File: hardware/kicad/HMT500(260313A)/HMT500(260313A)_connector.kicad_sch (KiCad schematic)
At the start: 10 parts, among them J1 SM08B-GHS-TB, J5 Chassis contact

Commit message: Schematic: global label shape shows signal direction (driver = output, receiver = input)
Direction derived per net from pin types (output / tri-state / open-drain
drivers, MCU as driver when only inputs are on the other side); analog
and passive nets keep the plain shape, RS-485 bus bidirectional.
Legend line on the root sheet; test for key nets.

Co-Authored-By: Claude Opus 5.5 <noreply@anthropic.com>
Claude-Session: https://claude.ai/code/session_01JA2o8uJsqp9Vzsg4b665ev
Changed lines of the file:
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@@
 (global_label "OUT1_EXT" (shape passive) (at 58.42 76.2 0) (fields_autoplaced) (effects (font (size 1.27 1.27)) (justify left)) (property "Intersheetrefs" "${INTERSHEET_REFS}" (at 58.42 76.2 0) (effects (font (size 1.27 1.27)) hide)))
 (global_label "OUT2_EXT" (shape passive) (at 58.42 78.74 0) (fields_autoplaced) (effects (font (size 1.27 1.27)) (justify left)) (property "Intersheetrefs" "${INTERSHEET_REFS}" (at 58.42 78.74 0) (effects (font (size 1.27 1.27)) hide)))
-(global_label "RS485_A_EXT" (shape passive) (at 58.42 81.28 0) (fields_autoplaced) (effects (font (size 1.27 1.27)) (justify left)) (property "Intersheetrefs" "${INTERSHEET_REFS}" (at 58.42 81.28 0) (effects (font (size 1.27 1.27)) hide)))
-(global_label "RS485_B_EXT" (shape passive) (at 58.42 83.82 0) (fields_autoplaced) (effects (font (size 1.27 1.27)) (justify left)) (property "Intersheetrefs" "${INTERSHEET_REFS}" (at 58.42 83.82 0) (effects (font (size 1.27 1.27)) hide)))
+(global_label "RS485_A_EXT" (shape bidirectional) (at 58.42 81.28 0) (fields_autoplaced) (effects (font (size 1.27 1.27)) (justify left)) (property "Intersheetrefs" "${INTERSHEET_REFS}" (at 58.42 81.28 0) (effects (font (size 1.27 1.27)) hide)))
+(global_label "RS485_B_EXT" (shape bidirectional) (at 58.42 83.82 0) (fields_autoplaced) (effects (font (size 1.27 1.27)) (justify left)) (property "Intersheetrefs" "${INTERSHEET_REFS}" (at 58.42 83.82 0) (effects (font (size 1.27 1.27)) hide)))
 (no_connect (at 55.88 86.36))
 (no_connect (at 55.88 88.9))

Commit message: Schematic: wire nearby same-sheet nets, signal-flow direction for analog nets
- Analog: +VSENSE and terminal feedback drawn as wires to the OPA197
  buffer (no DACn_SENSE / second OUTn_EXT labels); U14 1A/2A tied, one
  DAC_SCK label
- Power: TPS2660 left pins reordered so R3-R5 run straight from IN to
  UVLO/OVP; one VIN_F label
- Measurement: C27 sits directly between R17/R18 and AIN1/AIN2
- MCU: SWD pads (J2) placed on the PA13/PA14 rows and wired directly
- Label direction for passive nets from signal flow: OUTn_EXT analog ->
  connector, VIN_F connector -> eFuse, BUCK_FB divider -> FB
- Tests: nearby same-sheet labels must be wired; bend limit 6/sheet;
  check_netlist accepts KiCad auto-named multi-pin nets

Co-Authored-By: Claude Opus 5.5 <noreply@anthropic.com>
Claude-Session: https://claude.ai/code/session_01JA2o8uJsqp9Vzsg4b665ev
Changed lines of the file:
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@@
 (wire (pts (xy 137.16 114.3) (xy 137.16 116.84)) (stroke (width 0) (type default)))
 (wire (pts (xy 137.16 124.46) (xy 137.16 127)) (stroke (width 0) (type default)))
-(global_label "VIN_F" (shape passive) (at 182.88 71.12 0) (fields_autoplaced) (effects (font (size 1.27 1.27)) (justify left)) (property "Intersheetrefs" "${INTERSHEET_REFS}" (at 182.88 71.12 0) (effects (font (size 1.27 1.27)) hide)))
-(global_label "OUT1_EXT" (shape passive) (at 58.42 76.2 0) (fields_autoplaced) (effects (font (size 1.27 1.27)) (justify left)) (property "Intersheetrefs" "${INTERSHEET_REFS}" (at 58.42 76.2 0) (effects (font (size 1.27 1.27)) hide)))
-(global_label "OUT2_EXT" (shape passive) (at 58.42 78.74 0) (fields_autoplaced) (effects (font (size 1.27 1.27)) (justify left)) (property "Intersheetrefs" "${INTERSHEET_REFS}" (at 58.42 78.74 0) (effects (font (size 1.27 1.27)) hide)))
+(global_label "VIN_F" (shape output) (at 182.88 71.12 0) (fields_autoplaced) (effects (font (size 1.27 1.27)) (justify left)) (property "Intersheetrefs" "${INTERSHEET_REFS}" (at 182.88 71.12 0) (effects (font (size 1.27 1.27)) hide)))
+(global_label "OUT1_EXT" (shape input) (at 58.42 76.2 0) (fields_autoplaced) (effects (font (size 1.27 1.27)) (justify left)) (property "Intersheetrefs" "${INTERSHEET_REFS}" (at 58.42 76.2 0) (effects (font (size 1.27 1.27)) hide)))
+(global_label "OUT2_EXT" (shape input) (at 58.42 78.74 0) (fields_autoplaced) (effects (font (size 1.27 1.27)) (justify left)) (property "Intersheetrefs" "${INTERSHEET_REFS}" (at 58.42 78.74 0) (effects (font (size 1.27 1.27)) hide)))
 (global_label "RS485_A_EXT" (shape bidirectional) (at 58.42 81.28 0) (fields_autoplaced) (effects (font (size 1.27 1.27)) (justify left)) (property "Intersheetrefs" "${INTERSHEET_REFS}" (at 58.42 81.28 0) (effects (font (size 1.27 1.27)) hide)))
 (global_label "RS485_B_EXT" (shape bidirectional) (at 58.42 83.82 0) (fields_autoplaced) (effects (font (size 1.27 1.27)) (justify left)) (property "Intersheetrefs" "${INTERSHEET_REFS}" (at 58.42 83.82 0) (effects (font (size 1.27 1.27)) hide)))

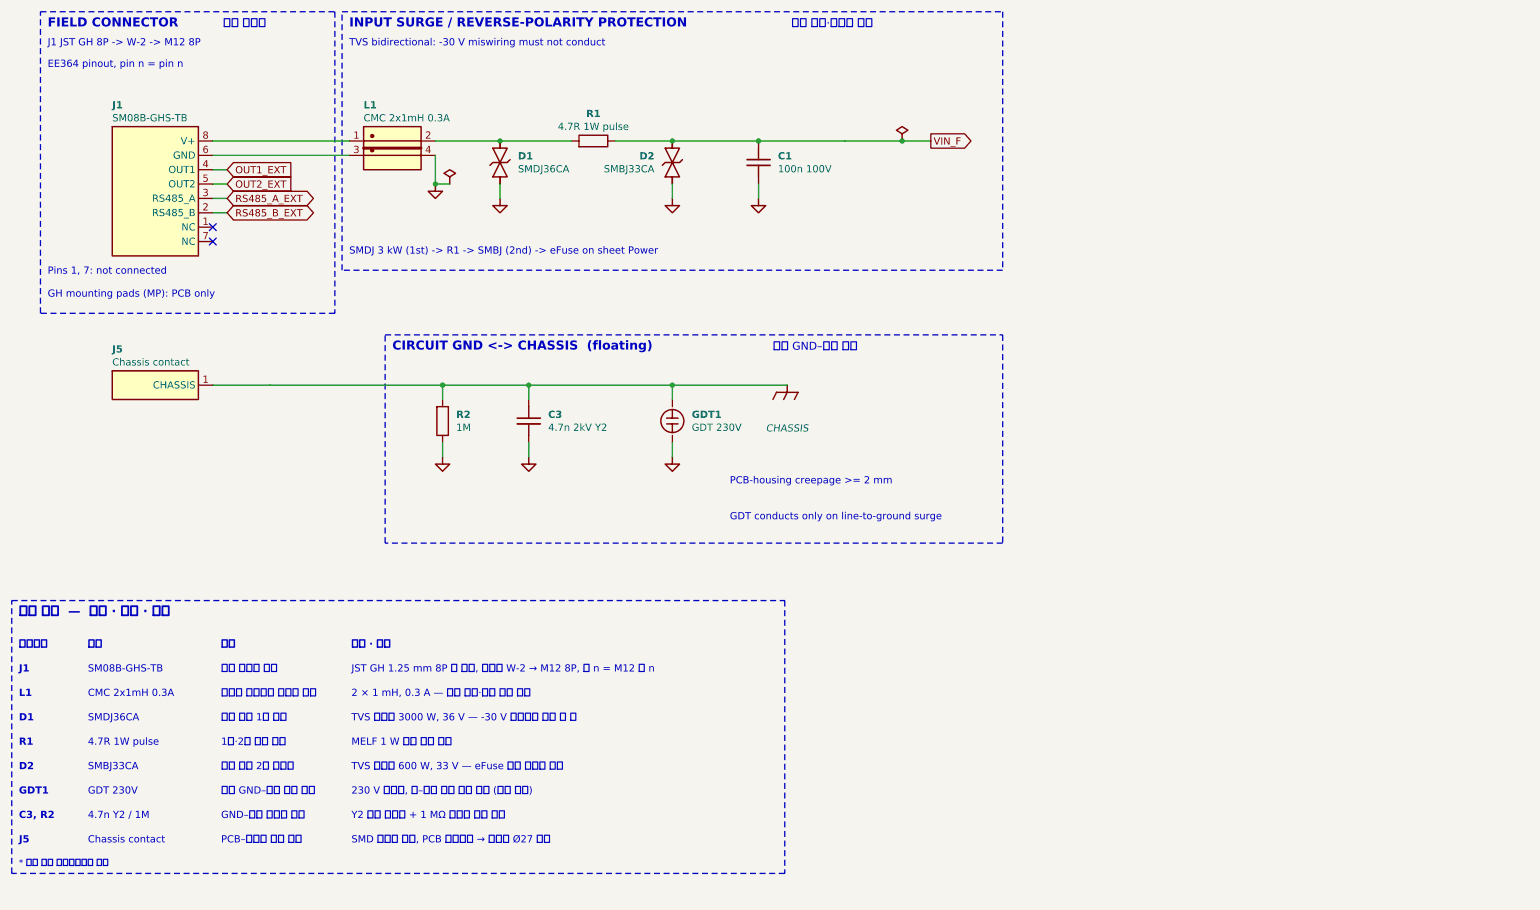
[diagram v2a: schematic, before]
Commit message: Footprints and part numbers: no TBD left in the schematic
- Project footprint library hardware/kicad/lib/HMT500_260313A.pretty:
  KiCad 7.0.11 footprints + gen_footprints.py (LMR36006 RNX0012A from TI
  land pattern, Bourns 2035-xx-SM GDT, TVS3301 DRB with floating pad)
- GDT changed to 2-electrode Bourns 2035-23-SM-RPLF (2038 is 3-electrode)
- L1 Wurth WE-SL2 744222 (1 mH, 0.8 A); CMC pins renumbered to WE-SL2
  windings 1-4 / 2-3
- J5 Harwin S1941-46R, L2 Coilcraft XGL4030-153MEC, TPS26611 SOT-23-8,
  TPS2660 HTSSOP-16 footprint from 7.0.11
- R1 MMB02070C4708FB200, R30/R40 CRCW251210R0FKEGHP confirmed;
  R19 -> Vishay PLTT0603 0.02 % 5 ppm
- fp-lib-table written by the generator; netlist 74/74, tests pass

Co-Authored-By: Claude Opus 5.5 <noreply@anthropic.com>
Claude-Session: https://claude.ai/code/session_01JA2o8uJsqp9Vzsg4b665ev
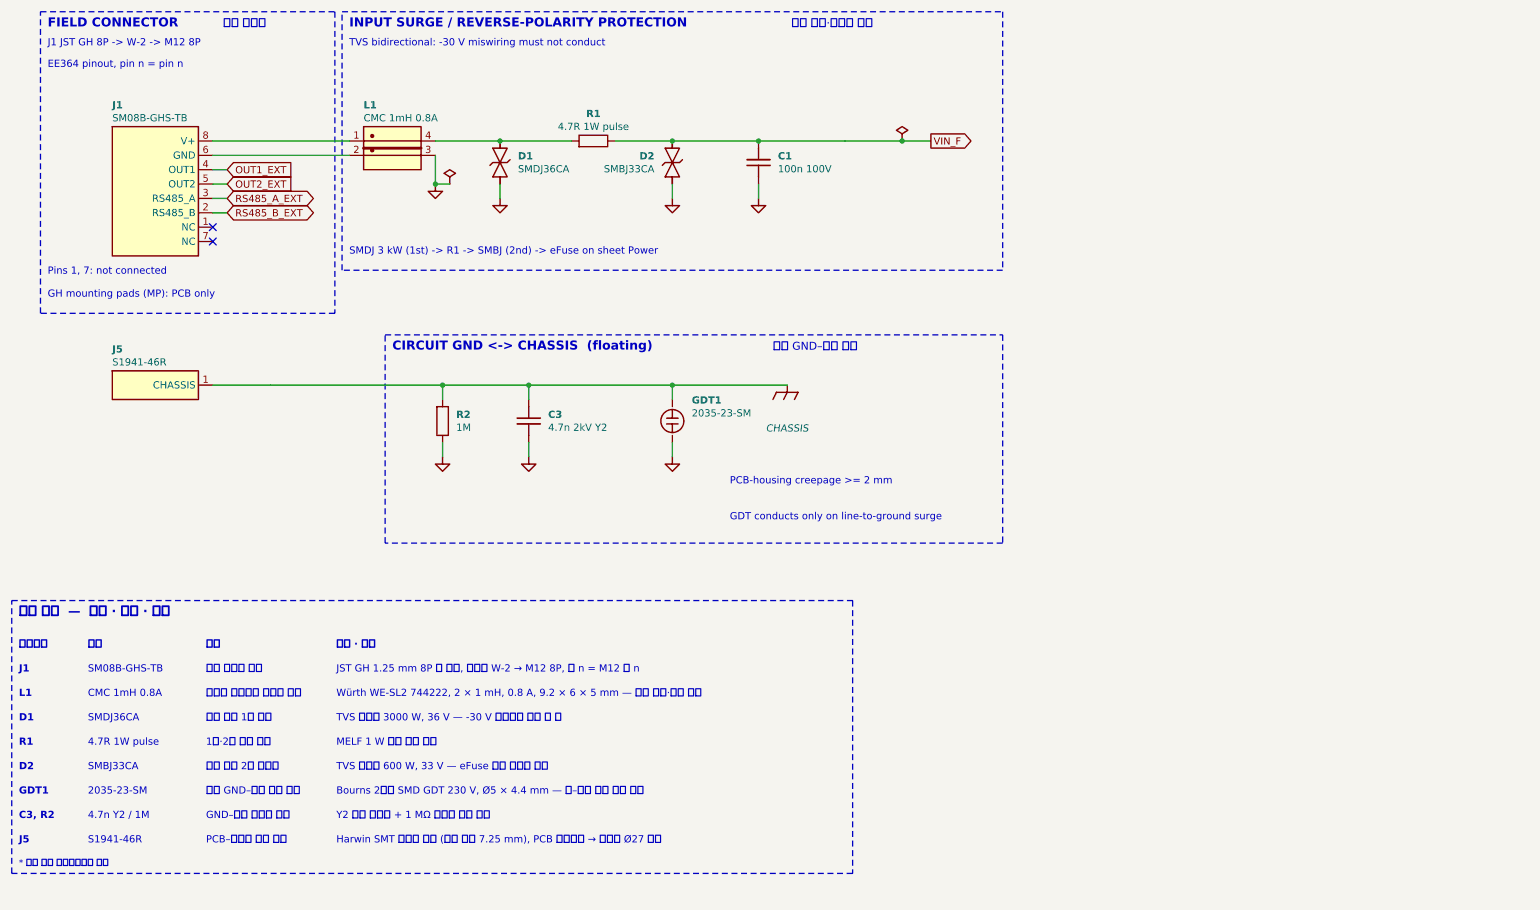
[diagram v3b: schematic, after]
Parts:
- GDT1: value GDT 230V -> 2035-23-SM; footprint TBD:GDT_Bourns_2038 -> HMT500_260313A:GDT_Bourns_2035-xx-SM
- J5: value Chassis contact -> S1941-46R; footprint TBD:Chassis_Spring_Contact -> Connector:SpringContact_Harwin_S1941-46R
- L1: value CMC 2x1mH 0.3A -> CMC 1mH 0.8A; footprint TBD:CMC_WE-SL -> Inductor_SMD:L_CommonMode_Wuerth_WE-SL2
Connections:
- net GND: now also L1.3; no longer L1.4
- net at D1.1, R1.1: now also L1.4; no longer L1.2
- net at J1.6 (GND): now also L1.2; no longer L1.3
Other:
- note added: "2035-23-SM"
- note added: "Bourns 2전극 SMD GDT 230 V, Ø5 × 4.4 mm — 선–대지 서지 때만 도통"
- note added: "CMC 1mH 0.8A"
- note added: "Harwin SMT 스프링 접점 (자유 높이 7.25 mm), PCB 가장자리 → 하우징 Ø27 내면"
- note added: "S1941-46R"
- note added: "Würth WE-SL2 744222, 2 × 1 mH, 0.8 A, 9.2 × 6 × 5 mm — 전도 방출·내성 대책"
- note removed: "2 × 1 mH, 0.3 A — 전도 방출·전도 내성 대책"
- note removed: "230 V 방전관, 선–대지 서지 때만 도통 (평소 절연)"
- note removed: "CMC 2x1mH 0.3A"
- note removed: "Chassis contact"
- note removed: "GDT 230V"
- note removed: "SMD 스프링 접점, PCB 가장자리 → 하우징 Ø27 내면"

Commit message: Apply assembly-simulation fixes A-F; re-simulation NG 0
- A: holder M-105 window 5.6 x 3.2 above the PCB slot (W-1 plug passes
  with the PCB already fitted); bench sub-assembly for the cross screws
- B: PCB wide section ends at x 63.4 (0.6 mm to the endcap face)
- C: placement height rule behind the ring (x >= 59) uses Ø20
- D: J5 spring contact removed; J5 = solder hole for a chassis wire to an
  M2 ring terminal under the holder top screw (M2x8, cbore Ø5.2 x 2.2);
  C3/R2 moved next to J5 (GDT1 mid-board, route CHASSIS wide)
- E: W-2 harness 60 -> 40 mm; top area behind J1 kept part-free
- F: assembly tool T-001 push bar (STEP for 3D printing)
- CAD reads the real PCB placement; drawings Rev G with the new sequence;
  simulation rewritten for the new sequence (23 checks, NG 0)
- Decision #27; docs updated

Co-Authored-By: Claude Opus 5.5 <noreply@anthropic.com>
Claude-Session: https://claude.ai/code/session_01JA2o8uJsqp9Vzsg4b665ev
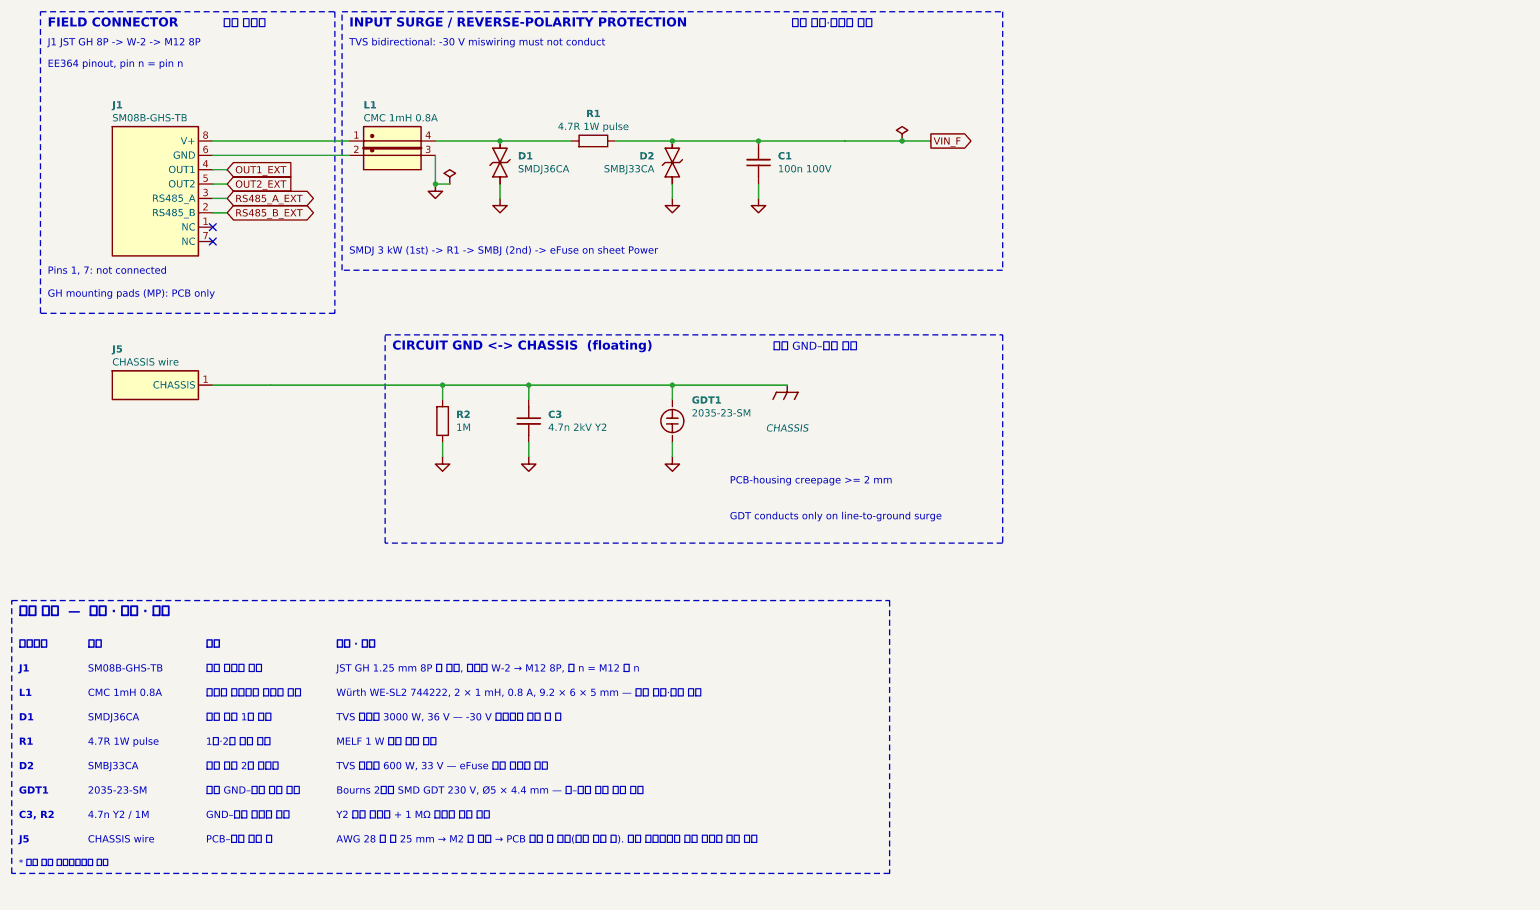
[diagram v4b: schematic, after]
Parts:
- J5: value S1941-46R -> CHASSIS wire; footprint Connector:SpringContact_Harwin_S1941-46R -> HMT500_260313A:SolderWire_Chassis_D0.6mm
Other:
- note added: "AWG 28 선 약 25 mm → M2 링 단자 → PCB 홀더 축 나사(금속 바디 탭). 조립 시뮬레이션 결과 스프링 접점 대체"
- note added: "CHASSIS wire"
- note added: "PCB–바디 접지 선"
- note removed: "Harwin SMT 스프링 접점 (자유 높이 7.25 mm), PCB 가장자리 → 하우징 Ø27 내면"
- note removed: "PCB–하우징 접지 접점"
- note removed: "S1941-46R"
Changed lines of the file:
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@@
 (symbol (lib_id "HMT500_260313A:GND") (at 152.4 81.28 0) (unit 1) (in_bom no) (on_board no) (dnp no) (property "Reference" "#PWR005" (at 152.4 87.63 0) (effects (font (size 1.27 1.27) bold) hide)) (property "Value" "GND" (at 152.4 88.9 0) (effects (font (size 1.27 1.27) italic) hide)) (property "Footprint" "" (at 152.4 81.28 0) (effects (font (size 1.27 1.27)) hide)) (property "Datasheet" "~" (at 152.4 81.28 0) (effects (font (size 1.27 1.27)) hide)) (pin "1") (instances (project "HMT500(260313A)" (path "/1ebb025b-11bd-5f7c-aaab-41e2a750e8b3/0bab42be-b4c8-521d-bf46-bb41b4d8556f" (reference "#PWR005") (unit 1)))))
 (symbol (lib_id "HMT500_260313A:PWR_FLAG") (at 177.8 71.12 0) (unit 1) (in_bom no) (on_board no) (dnp no) (property "Reference" "#FLG006" (at 177.8 62.992 0) (effects (font (size 1.27 1.27) bold) hide)) (property "Value" "PWR_FLAG" (at 177.8 65.278 0) (effects (font (size 1.27 1.27)) hide)) (property "Footprint" "" (at 177.8 71.12 0) (effects (font (size 1.27 1.27)) hide)) (property "Datasheet" "~" (at 177.8 71.12 0) (effects (font (size 1.27 1.27)) hide)) (pin "1") (instances (project "HMT500(260313A)" (path "/1ebb025b-11bd-5f7c-aaab-41e2a750e8b3/0bab42be-b4c8-521d-bf46-bb41b4d8556f" (reference "#FLG006") (unit 1)))))
-(symbol (lib_id "HMT500_260313A:CONN_CH") (at 45.72 114.3 0) (unit 1) (in_bom yes) (on_board yes) (dnp no) (property "Reference" "J5" (at 38.1 107.95 0) (effects (font (size 1.27 1.27) bold) (justify left))) (property "Value" "S1941-46R" (at 38.1 110.236 0) (effects (font (size 1.27 1.27)) (justify left))) (property "Footprint" "Connector:SpringContact_Harwin_S1941-46R" (at 45.72 114.3 0) (effects (font (size 1.27 1.27)) hide)) (property "Datasheet" "~" (at 45.72 114.3 0) (effects (font (size 1.27 1.27)) hide)) (pin "1") (instances (project "HMT500(260313A)" (path "/1ebb025b-11bd-5f7c-aaab-41e2a750e8b3/0bab42be-b4c8-521d-bf46-bb41b4d8556f" (reference "J5") (unit 1)))))
+(symbol (lib_id "HMT500_260313A:CONN_CH") (at 45.72 114.3 0) (unit 1) (in_bom yes) (on_board yes) (dnp no) (property "Reference" "J5" (at 38.1 107.95 0) (effects (font (size 1.27 1.27) bold) (justify left))) (property "Value" "CHASSIS wire" (at 38.1 110.236 0) (effects (font (size 1.27 1.27)) (justify left))) (property "Footprint" "HMT500_260313A:SolderWire_Chassis_D0.6mm" (at 45.72 114.3 0) (effects (font (size 1.27 1.27)) hide)) (property "Datasheet" "~" (at 45.72 114.3 0) (effects (font (size 1.27 1.27)) hide)) (pin "1") (instances (project "HMT500(260313A)" (path "/1ebb025b-11bd-5f7c-aaab-41e2a750e8b3/0bab42be-b4c8-521d-bf46-bb41b4d8556f" (reference "J5") (unit 1)))))
 (symbol (lib_id "HMT500_260313A:R") (at 96.52 120.65 0) (unit 1) (in_bom yes) (on_board yes) (dnp no) (property "Reference" "R2" (at 98.933 119.507 0) (effects (font (size 1.27 1.27) bold) (justify left))) (property "Value" "1M" (at 98.933 121.793 0) (effects (font (size 1.27 1.27)) (justify left))) (property "Footprint" "Resistor_SMD:R_0603_1608Metric" (at 96.52 120.65 0) (effects (font (size 1.27 1.27)) hide)) (property "Datasheet" "~" (at 96.52 120.65 0) (effects (font (size 1.27 1.27)) hide)) (pin "1") (pin "2") (instances (project "HMT500(260313A)" (path "/1ebb025b-11bd-5f7c-aaab-41e2a750e8b3/0bab42be-b4c8-521d-bf46-bb41b4d8556f" (reference "R2") (unit 1)))))
 (symbol (lib_id "HMT500_260313A:C") (at 111.76 120.65 0) (unit 1) (in_bom yes) (on_board yes) (dnp no) (property "Reference" "C3" (at 115.189 119.507 0) (effects (font (size 1.27 1.27) bold) (justify left))) (property "Value" "4.7n 2kV Y2" (at 115.189 121.793 0) (effects (font (size 1.27 1.27)) (justify left))) (property "Footprint" "Capacitor_SMD:C_1812_4532Metric" (at 111.76 120.65 0) (effects (font (size 1.27 1.27)) hide)) (property "Datasheet" "~" (at 111.76 120.65 0) (effects (font (size 1.27 1.27)) hide)) (pin "1") (pin "2") (instances (project "HMT500(260313A)" (path "/1ebb025b-11bd-5f7c-aaab-41e2a750e8b3/0bab42be-b4c8-521d-bf46-bb41b4d8556f" (reference "C3") (unit 1)))))
@@
 (rectangle (start 78.74 48.26) (end 195.58 93.98) (stroke (width 0.1524) (type dash) (color 72 72 160 1)) (fill (type none)))
 (rectangle (start 86.36 105.41) (end 195.58 142.24) (stroke (width 0.1524) (type dash) (color 72 72 160 1)) (fill (type none)))
-(rectangle (start 20.32 152.4) (end 169.042 200.66) (stroke (width 0.1524) (type dash) (color 72 72 160 1)) (fill (type none)))
+(rectangle (start 20.32 152.4) (end 175.583 200.66) (stroke (width 0.1524) (type dash) (color 72 72 160 1)) (fill (type none)))
 (text "FIELD CONNECTOR" (at 26.67 51.308 0) (effects (font (size 1.6 1.6) bold) (justify left bottom)))
 (text "현장 커넥터" (at 57.696 51.308 0) (effects (font (face "NanumGothic") (size 1.4 1.4)) (justify left bottom)))
@@
 (text "Y2 안전 콘덴서 + 1 MΩ 정전기 방전 경로" (at 77.7291 191.262 0) (effects (font (face "NanumGothic") (size 1.27 1.27)) (justify left bottom)))
 (text "J5" (at 21.59 195.58 0) (effects (font (size 1.27 1.27) bold) (justify left bottom)))
-(text "S1941-46R" (at 33.7871 195.58 0) (effects (font (size 1.27 1.27)) (justify left bottom)))
-(text "PCB–하우징 접지 접점" (at 54.6786 195.58 0) (effects (font (face "NanumGothic") (size 1.27 1.27)) (justify left bottom)))
-(text "Harwin SMT 스프링 접점 (자유 높이 7.25 mm), PCB 가장자리 → 하우징 Ø27 내면" (at 77.7291 195.58 0) (effects (font (face "NanumGothic") (size 1.27 1.27)) (justify left bottom)))
+(text "CHASSIS wire" (at 33.7871 195.58 0) (effects (font (size 1.27 1.27)) (justify left bottom)))
+(text "PCB–바디 접지 선" (at 54.6786 195.58 0) (effects (font (face "NanumGothic") (size 1.27 1.27)) (justify left bottom)))
+(text "AWG 28 선 약 25 mm → M2 링 단자 → PCB 홀더 축 나사(금속 바디 탭). 조립 시뮬레이션 결과 스프링 접점 대체" (at 77.7291 195.58 0) (effects (font (face "NanumGothic") (size 1.27 1.27)) (justify left bottom)))
 (text "주요 부품  —  역할 · 특징 · 사양" (at 21.59 155.448 0) (effects (font (face "NanumGothic") (size 1.6 1.6) bold) (justify left bottom)))
 (text "* 표시 값은 데이터시트로 확인" (at 21.59 199.644 0) (effects (font (face "NanumGothic") (size 1.1 1.1)) (justify left bottom)))
